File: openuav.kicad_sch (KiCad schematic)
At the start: 29 parts, among them J1 UART_3, J10 PROG, J2 Conn_01x02, J3 ESC_1, J4 UART_1, J5 ESC_2, J6 UART_2, J7 ESC_3, J8 UART_3, J9 ESC_4, U1 STM32G431CBUx, U3 LSM6DSR, U4 LPS22HH, U5 L78L33_SOT89

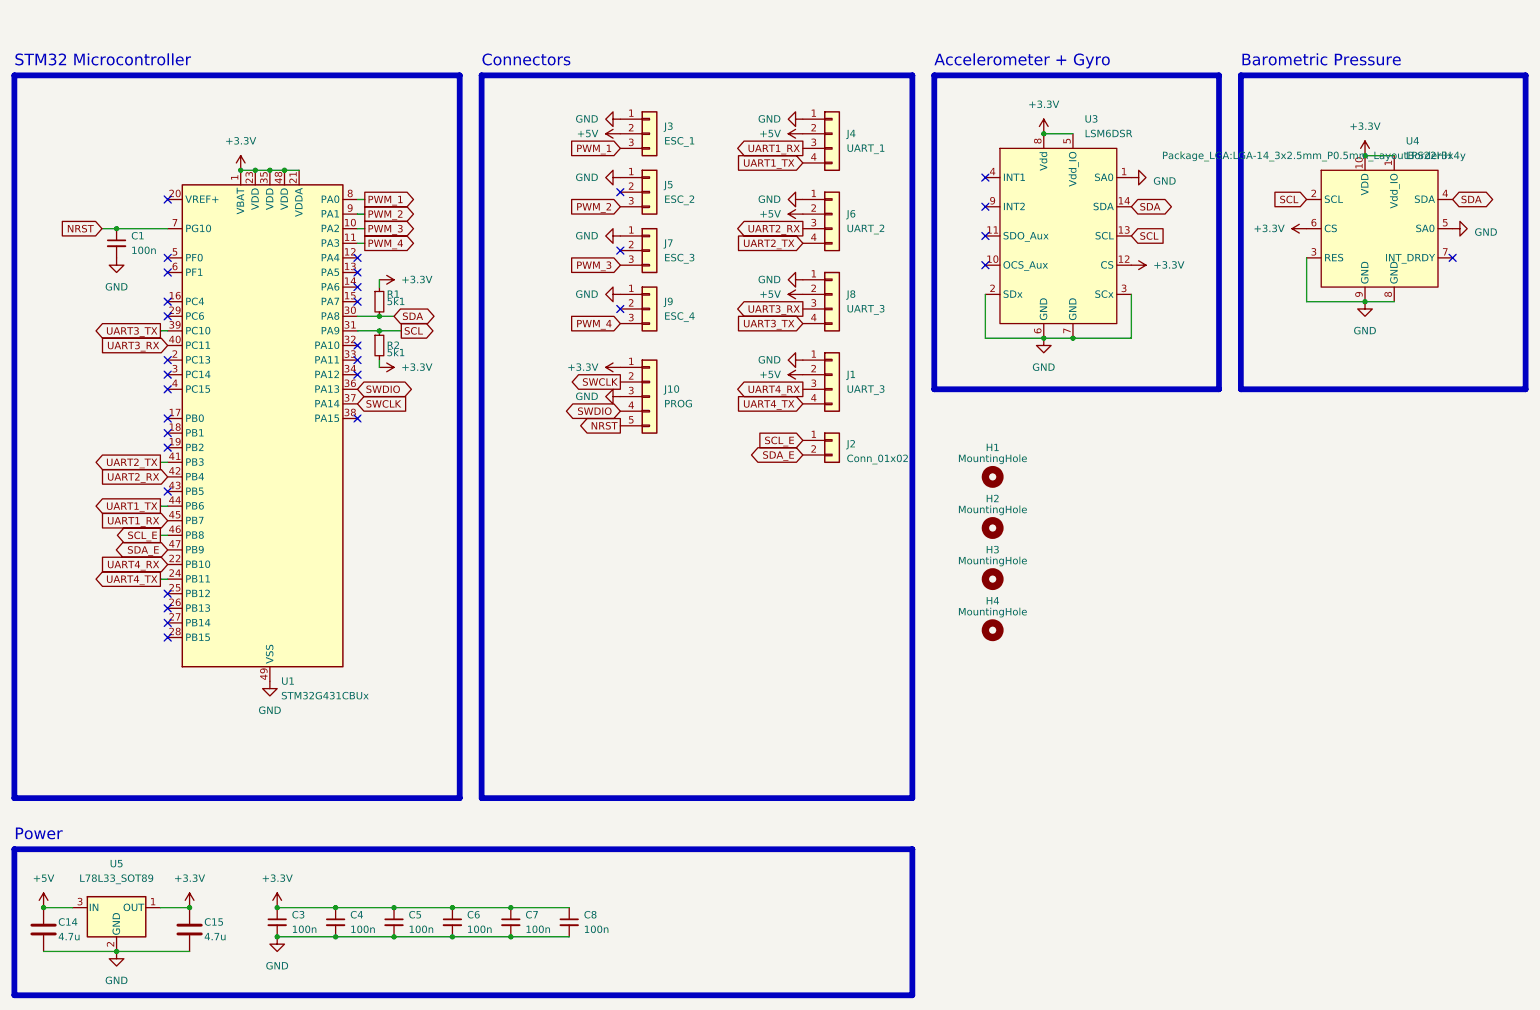
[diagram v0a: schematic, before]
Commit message: Work in progress on more complete schematic
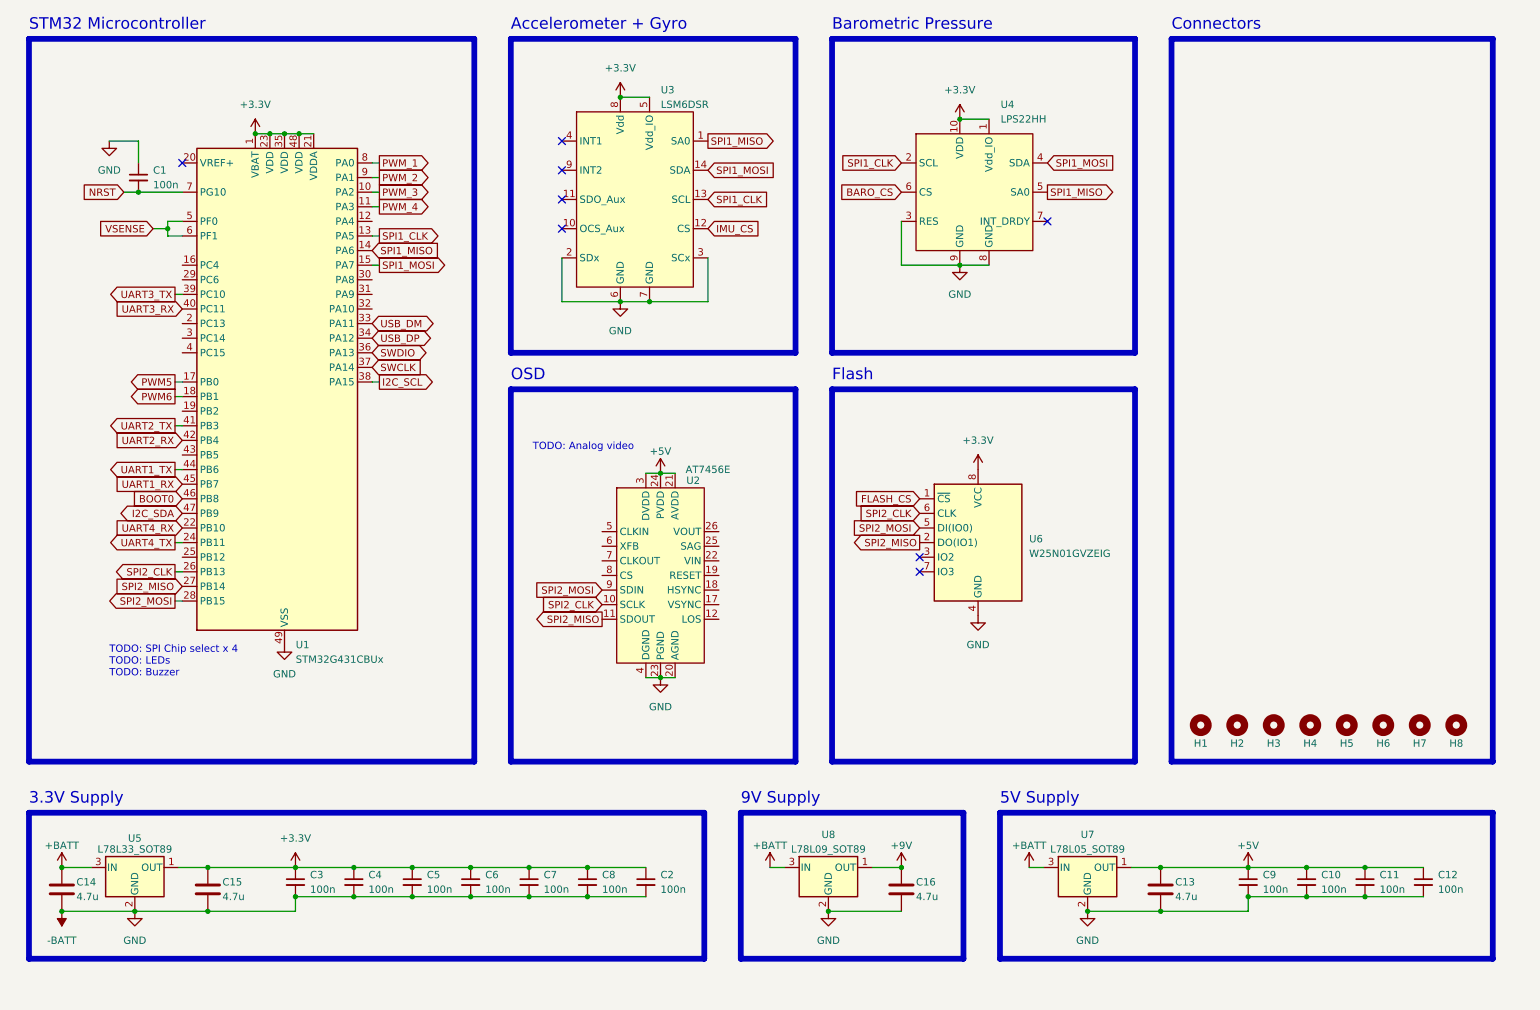
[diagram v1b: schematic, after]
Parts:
- removed J1, J8: UART_3, Connector_PinHeader_2.54mm:PinHeader_1x04_P2.54mm_Vertical, symbol Connector_Generic:Conn_01x04
- removed J10: PROG, Connector_PinHeader_2.54mm:PinHeader_1x05_P2.54mm_Vertical, symbol Connector_Generic:Conn_01x05
- removed J2: Conn_01x02, Connector_PinHeader_2.54mm:PinHeader_1x02_P2.54mm_Vertical, symbol Connector_Generic:Conn_01x02
- removed J3: ESC_1, Connector_PinHeader_2.54mm:PinHeader_1x03_P2.54mm_Vertical, symbol Connector_Generic:Conn_01x03
- removed J4: UART_1, Connector_PinHeader_2.54mm:PinHeader_1x04_P2.54mm_Vertical, symbol Connector_Generic:Conn_01x04
- removed J5: ESC_2, Connector_PinHeader_2.54mm:PinHeader_1x03_P2.54mm_Vertical, symbol Connector_Generic:Conn_01x03
- removed J6: UART_2, Connector_PinHeader_2.54mm:PinHeader_1x04_P2.54mm_Vertical, symbol Connector_Generic:Conn_01x04
- removed J7: ESC_3, Connector_PinHeader_2.54mm:PinHeader_1x03_P2.54mm_Vertical, symbol Connector_Generic:Conn_01x03
- removed J9: ESC_4, Connector_PinHeader_2.54mm:PinHeader_1x03_P2.54mm_Vertical, symbol Connector_Generic:Conn_01x03
- removed R1, R2: 5k1, Resistor_SMD:R_0402_1005Metric, symbol Device:R_Small
- added C10, C11, C12, C2, C9: 100n, Capacitor_SMD:C_0402_1005Metric, symbol Device:C_Small
- added C13, C16: 4.7u, Capacitor_SMD:C_0603_1608Metric, symbol Device:C
- added H5, H6, H7, H8: MountingHole, MountingHole:MountingHole_3.2mm_M3, symbol Mechanical:MountingHole
- added U2: AT7456E, Package_SO:TSSOP-28-1EP_4.4x9.7mm_P0.65mm_EP2.85x6.7mm, symbol Max_Video:AT7456E
- added U6: W25N01GVZEIG, Package_SON:WSON-8-1EP_8x6mm_P1.27mm_EP3.4x4.3mm, symbol Memory_Flash:W25Q32JVSS
- added U7: L78L05_SOT89, Package_TO_SOT_SMD:SOT-89-3, symbol Regulator_Linear:L78L05_SOT89
- added U8: L78L09_SOT89, Package_TO_SOT_SMD:SOT-89-3, symbol Regulator_Linear:L78L09_SOT89
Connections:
- net +3V3: now also C2.1, U6.8 (VCC); no longer U3.12 (CS), U4.6 (CS)
- net +5V: now also C10.1, C11.1, C12.1, C13.1, C9.1, U2.21 (AVDD), U2.24 (PVDD), U2.3 (DVDD), U7.1 (OUT); no longer C14.1, U5.3 (IN)
- net NRST: now also C1.2; no longer C1.1
- net SPI1_CLK: now reaches U1.13 (PA5)
- net SPI1_CLK: now also U3.13 (SCL), U4.2 (SCL)
- net SPI1_MISO: now reaches U1.14 (PA6)
- net SPI1_MISO: now also U3.1 (SA0), U4.5 (SA0)
- net SPI1_MOSI: now reaches U1.15 (PA7)
- net SPI1_MOSI: now also U3.14 (SDA), U4.4 (SDA)
- net PWM5: now reaches U1.17 (PB0)
- net PWM6: now reaches U1.18 (PB1)
- net SPI2_CLK: now reaches U1.26 (PB13)
- net SPI2_CLK: now also U2.10 (SCLK), U6.6 (CLK)
- net SPI2_MISO: now reaches U1.27 (PB14)
- net SPI2_MISO: now also U2.11 (SDOUT), U6.2 (DO(IO1))
- net SPI2_MOSI: now reaches U1.28 (PB15)
- net SPI2_MOSI: now also U2.9 (SDIN), U6.5 (DI(IO0))
- net USB_DM: now reaches U1.33 (PA11)
- net USB_DP: now reaches U1.34 (PA12)
- net I2C_SCL: now reaches U1.38 (PA15)
- net VSENSE: now reaches U1.5 (PF0)
- net VSENSE: now also U1.6 (PF1)
- net GND renamed -BATT
- net -BATT: now also C1.1, C10.2, C11.2, C12.2, C13.2, C16.2, C2.2, C9.2, U2.20 (AGND), U2.23 (PGND), U2.4 (DGND), U6.4 (GND), U7.2 (GND), U8.2 (GND); no longer C1.2, U3.1 (SA0), U4.5 (SA0)
- removed net SCL: U1.31 (PA9), U3.13 (SCL), U4.2 (SCL)
- net SCL_E renamed BOOT0
- removed net SDA: U1.30 (PA8), U3.14 (SDA), U4.4 (SDA)
- net SDA_E renamed I2C_SDA
- new net +9V: C16.1, U8.1 (OUT)
- new net +BATT: C14.1, U5.3 (IN), U7.3 (IN), U8.3 (IN)
- new net BARO_CS: U4.6 (CS)
- new net FLASH_CS: U6.1 (~{CS})
- new net IMU_CS: U3.12 (CS)
- no-connect marks 32 -> 8
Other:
- note added: "3.3V Supply"
- note added: "5V Supply"
- note added: "9V Supply"
- note added: "Flash"
- note added: "OSD"
- note added: "TODO: Analog video"
- note added: "TODO: SPI Chip select x 4 TODO: LEDs TODO: Buzzer"
- note removed: "Power"
- moved on the sheet: C1, C14, C15, C3, C4, C5, C6, C7, C8, H1, H2, H3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

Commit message: Continued work in progress on initial design
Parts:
- removed C14: 4.7u, Capacitor_SMD:C_0603_1608Metric, symbol Device:C
- removed C9: 100n, Capacitor_SMD:C_0402_1005Metric, symbol Device:C_Small
- added D1: D_Schottky_Small, symbol Device:D_Schottky_Small
- added J1, J10, J11, J12, J13, J14, J15, J16, J17, J18, J19, J2, J20, J21, J22, J23, J25, J26, J3, J4, J5, J6, J7, J8, J9: Conn_01x01, TestPoint:TestPoint_Pad_2.0x2.0mm, symbol Connector_Generic:Conn_01x01
- added J99: USB_C_Receptacle_USB2.0, Connector_USB:USB_C_Receptacle_XKB_U262-16XN-4BVC11, symbol Connector:USB_C_Receptacle_USB2.0
- added R1, R2: 5k1, symbol Device:R_Small
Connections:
- net +5V: now also U5.3 (IN), D1.1 (K)
- net +9V: now also J26.1 (Pin_1)
- net +BATT: now also J23.1 (Pin_1); no longer U5.3 (IN)
- net BOOT0: now also J17.1 (Pin_1)
- net I2C_SCL: now also J15.1 (Pin_1)
- net I2C_SDA: now also J16.1 (Pin_1)
- net PWM_1: now also J1.1 (Pin_1)
- net PWM_2: now also J2.1 (Pin_1)
- net PWM_3: now also J3.1 (Pin_1)
- net PWM_4: now also J4.1 (Pin_1)
- net SPI1_CLK: no longer U1.13 (PA5)
- net SPI1_MISO: no longer U1.14 (PA6)
- net SPI1_MOSI: no longer U1.15 (PA7)
- net SPI2_CLK: no longer U1.26 (PB13)
- net SPI2_MISO: no longer U1.27 (PB14)
- net SPI2_MOSI: no longer U1.28 (PB15)
- net SWCLK: now also J21.1 (Pin_1)
- net SWDIO: now also J22.1 (Pin_1)
- net USB_DM: now also J99.A7 (D-), J99.B7 (D-)
- net USB_DP: now also J99.A6 (D+), J99.B6 (D+)
- net -BATT renamed GND
- net GND: now also J25.1 (Pin_1), J99.A1 (GND), J99.A12 (GND), J99.B1 (GND), J99.B12 (GND), J99.S1 (SHIELD), R1.2, R2.2
- net PWM5 renamed PWM_5
- net PWM_5: now also J5.1 (Pin_1)
- net PWM6 renamed PWM_6
- net PWM_6: now also J6.1 (Pin_1)
- net UART1_RX renamed UART_1_RX
- net UART_1_RX: now also J8.1 (Pin_1)
- net UART1_TX renamed UART_1_TX
- net UART_1_TX: now also J7.1 (Pin_1)
- net UART2_RX renamed UART_2_RX
- net UART_2_RX: now also J10.1 (Pin_1)
- net UART2_TX renamed UART_2_TX
- net UART_2_TX: now also J9.1 (Pin_1)
- net UART3_RX renamed UART_3_RX
- net UART_3_RX: now also J12.1 (Pin_1)
- net UART3_TX renamed UART_3_TX
- net UART_3_TX: now also J11.1 (Pin_1)
- net UART4_RX renamed UART_4_RX
- net UART_4_RX: now also J14.1 (Pin_1)
- net UART4_TX renamed UART_4_TX
- net UART_4_TX: now also J13.1 (Pin_1)
- new net: J99.B5 (CC2), R1.1
- new net: J99.A5 (CC1), R2.1
- new net: D1.2 (A), J99.A4 (VBUS), J99.A9 (VBUS), J99.B4 (VBUS), J99.B9 (VBUS)
- new net BUZZER: J18.1 (Pin_1)
- new net CAMERA: J19.1 (Pin_1)
- new net SPI_1_CLK: U1.13 (PA5)
- new net SPI_1_MISO: U1.14 (PA6)
- new net SPI_1_MOSI: U1.15 (PA7)
- new net SPI_2_CLK: U1.26 (PB13)
- new net SPI_2_MISO: U1.27 (PB14)
- new net SPI_2_MOSI: U1.28 (PB15)
- new net VIDEO: J20.1 (Pin_1)
- no-connect marks 8 -> 10
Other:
- note added: "TODO: SPI Chip select x 4 TODO: LEDs TODO: Buzzer These GPIOs will be chosen during layout"
- note added: "USB-C 2.0"
- note removed: "TODO: SPI Chip select x 4 TODO: LEDs TODO: Buzzer"
- moved on the sheet: C10, C11, C12, C13, C15, C16, C2, C3, C4, C5, C6, C7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

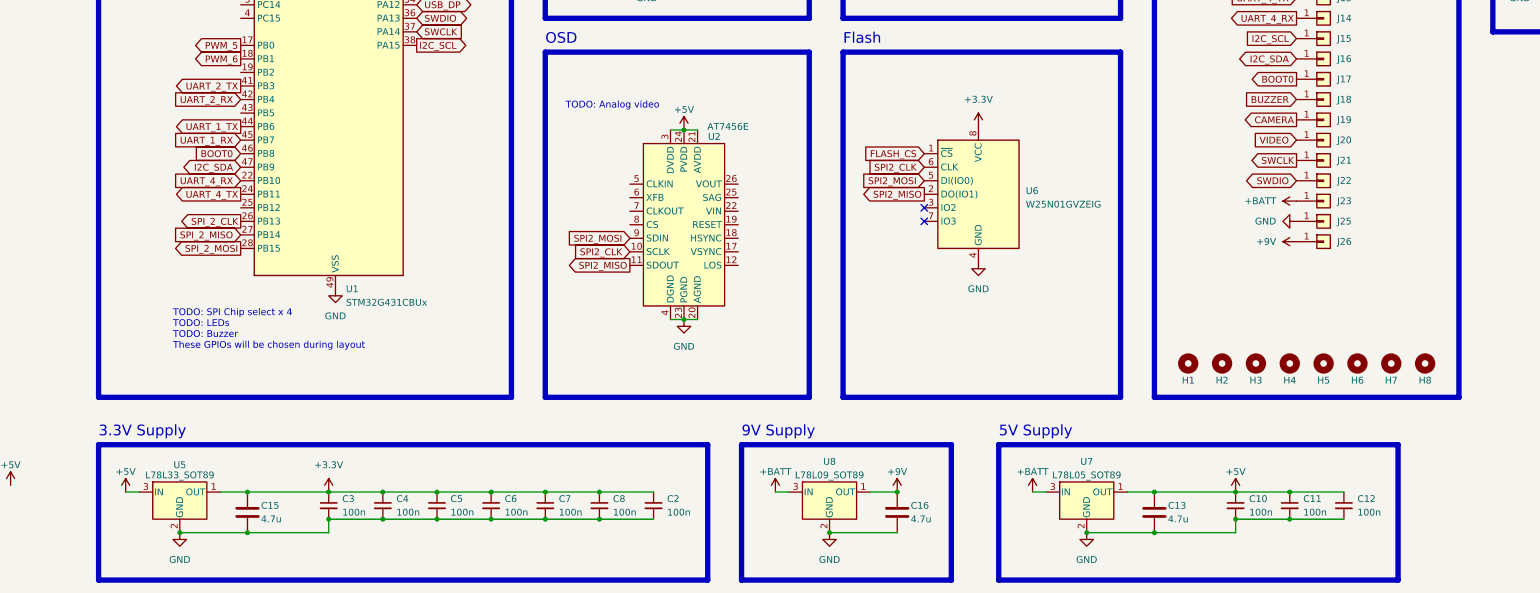
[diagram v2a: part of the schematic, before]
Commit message: Change OSD to 3v3, align pads to edge
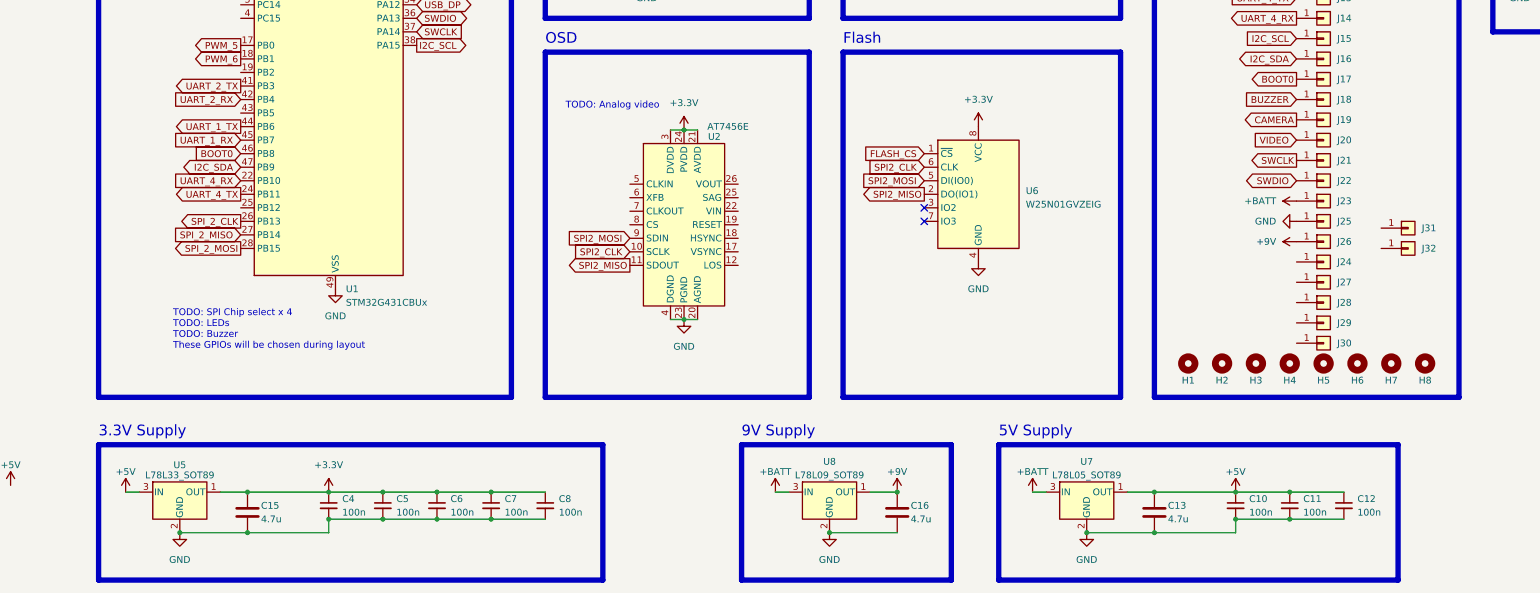
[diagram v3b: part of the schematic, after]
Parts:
- removed C2, C3: 100n, Capacitor_SMD:C_0402_1005Metric, symbol Device:C_Small
- added J24, J27, J28, J29, J30, J31, J32: Conn_01x01, TestPoint:TestPoint_Pad_2.0x2.0mm, symbol Connector_Generic:Conn_01x01
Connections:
- net +3V3: now also U2.21 (AVDD), U2.24 (PVDD), U2.3 (DVDD)
- net +5V: no longer U2.21 (AVDD), U2.24 (PVDD), U2.3 (DVDD)
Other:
- moved on the sheet: C4, C5, C6, C7, C8

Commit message: start to rethink power supplies
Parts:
- removed C10: 100n, Capacitor_SMD:C_0402_1005Metric, symbol Device:C_Small
- removed C13, C16: 4.7u, Capacitor_SMD:C_0603_1608Metric, symbol Device:C
- removed H5, H6, H7, H8: MountingHole, MountingHole:MountingHole_3.2mm_M3, symbol Mechanical:MountingHole
- removed U7: L78L05_SOT89, Package_TO_SOT_SMD:SOT-89-3, symbol Regulator_Linear:L78L05_SOT89
- removed U8: L78L09_SOT89, Package_TO_SOT_SMD:SOT-89-3, symbol Regulator_Linear:L78L09_SOT89
- added C2: 4.7u, Capacitor_SMD:C_0603_1608Metric, symbol Device:C
- added L1: IHLP4040DZER220M11, Inductor_SMD:L_Vishay_IHLP-4040, symbol Device:L
- added R3: 68k, Resistor_SMD:R_0402_1005Metric, symbol Device:R
- added R4: 10k, Resistor_SMD:R_0402_1005Metric, symbol Device:R
- added U7: TPS5430DDA, Package_SO:TI_SO-PowerPAD-8_ThermalVias, symbol Regulator_Switching:TPS5430DDA
- J1, J10, J11, J12, J13, J14, J15, J16, J17, J18, J19, J2, J20, J21, J22, J23, J24, J25, J26, J27, J28, J29, J3, J30, J31, J32, J4, J5, J6, J7, J8, J9: footprint TestPoint:TestPoint_Pad_2.0x2.0mm -> Connector_Custom_Pads:TestPoint_Pad_2.0x3.0mm
- R1, R2: footprint (none) -> Resistor_SMD:R_0402_1005Metric
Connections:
- net SPI1_CLK is gone; now on net SPI_1_CLK: U3.13 (SCL), U4.2 (SCL)
- net SPI1_MISO is gone; now on net SPI_1_MISO: U3.1 (SA0), U4.5 (SA0)
- net SPI1_MOSI is gone; now on net SPI_1_MOSI: U3.14 (SDA), U4.4 (SDA)
- net +3V3: now also C11.1, C12.1
- net +5V: no longer C11.1, C12.1
- net +9V: no longer J26.1 (Pin_1)
- net +BATT: now also C2.1, R3.1; no longer J23.1 (Pin_1)
- net BARO_CS: now also U1.12 (PA4)
- net BOOT0: no longer J17.1 (Pin_1)
- net BUZZER: no longer J18.1 (Pin_1)
- net CAMERA: no longer J19.1 (Pin_1)
- net FLASH_CS: now also U1.19 (PB2)
- net GND: now also C2.2, R4.1; no longer J25.1 (Pin_1)
- net I2C_SCL: no longer J15.1 (Pin_1)
- net I2C_SDA: no longer J16.1 (Pin_1)
- net IMU_CS: now also U1.16 (PC4)
- net PWM_1: no longer J1.1 (Pin_1)
- net PWM_2: no longer J2.1 (Pin_1)
- net PWM_3: no longer J3.1 (Pin_1)
- net PWM_4: no longer J4.1 (Pin_1)
- net PWM_5: no longer J5.1 (Pin_1)
- net PWM_6: no longer J6.1 (Pin_1)
- net SPI2_CLK: no longer U6.6 (CLK)
- net SPI2_MISO: no longer U6.2 (DO(IO1))
- net SPI2_MOSI: no longer U6.5 (DI(IO0))
- net SPI_2_CLK: now also U6.6 (CLK)
- net SPI_2_MISO: now also U6.2 (DO(IO1))
- net SPI_2_MOSI: now also U6.5 (DI(IO0))
- net SWCLK: no longer J21.1 (Pin_1)
- net SWDIO: no longer J22.1 (Pin_1)
- net UART_1_RX: no longer J8.1 (Pin_1)
- net UART_1_TX: no longer J7.1 (Pin_1)
- net UART_2_RX: no longer J10.1 (Pin_1)
- net UART_2_TX: no longer J9.1 (Pin_1)
- net UART_3_RX: no longer J12.1 (Pin_1)
- net UART_3_TX: no longer J11.1 (Pin_1)
- net UART_4_RX: no longer J14.1 (Pin_1)
- net UART_4_TX: no longer J13.1 (Pin_1)
- net VIDEO: no longer J20.1 (Pin_1)
- net VSENSE: now also R3.2, R4.2
- net OSD_CS: now reaches U2.8 (CS)
- net OSD_CS: now also U1.29 (PC6)
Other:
- note added: "6S x 4.2V => 3.3V"
- note added: "Battery Voltage Sense"
- note removed: "5V Supply"
- note removed: "9V Supply"
- moved on the sheet: C11, C12, H1, H2, H3, H4, U4, U6
